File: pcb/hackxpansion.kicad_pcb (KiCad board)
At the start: 2 copper layers, 376 x 59.8 mm, 80 parts, among them CN1 533981471, CN2 533981471, CN3 533981471, CN4 533981471, IC1 ADS7128IRTET, J1 Conn_01x03_MountingPin, J2 USB_C_Receptacle_USB2.0_14P, Q1 BSS138, Q2 2N7002, SW1 SW_Push, SW2 SW_Push, SW3 SW_On_Off, U2 RP2354B, U5 SPX3819M5-L-3-3, U7 BQ24075RGT, Y1 ABM8-272-T3

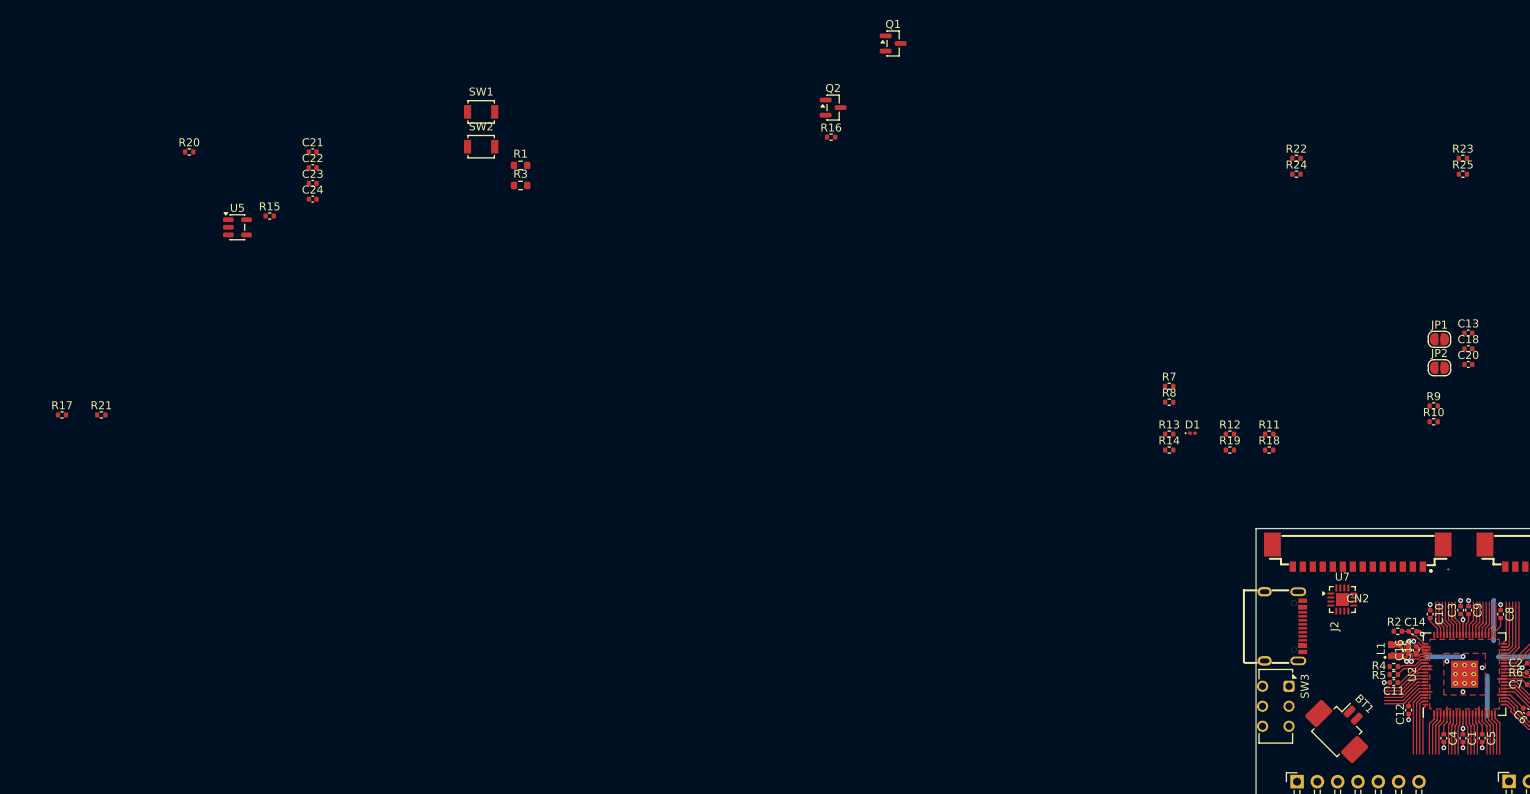
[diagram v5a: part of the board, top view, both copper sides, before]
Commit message: organized unlaid components
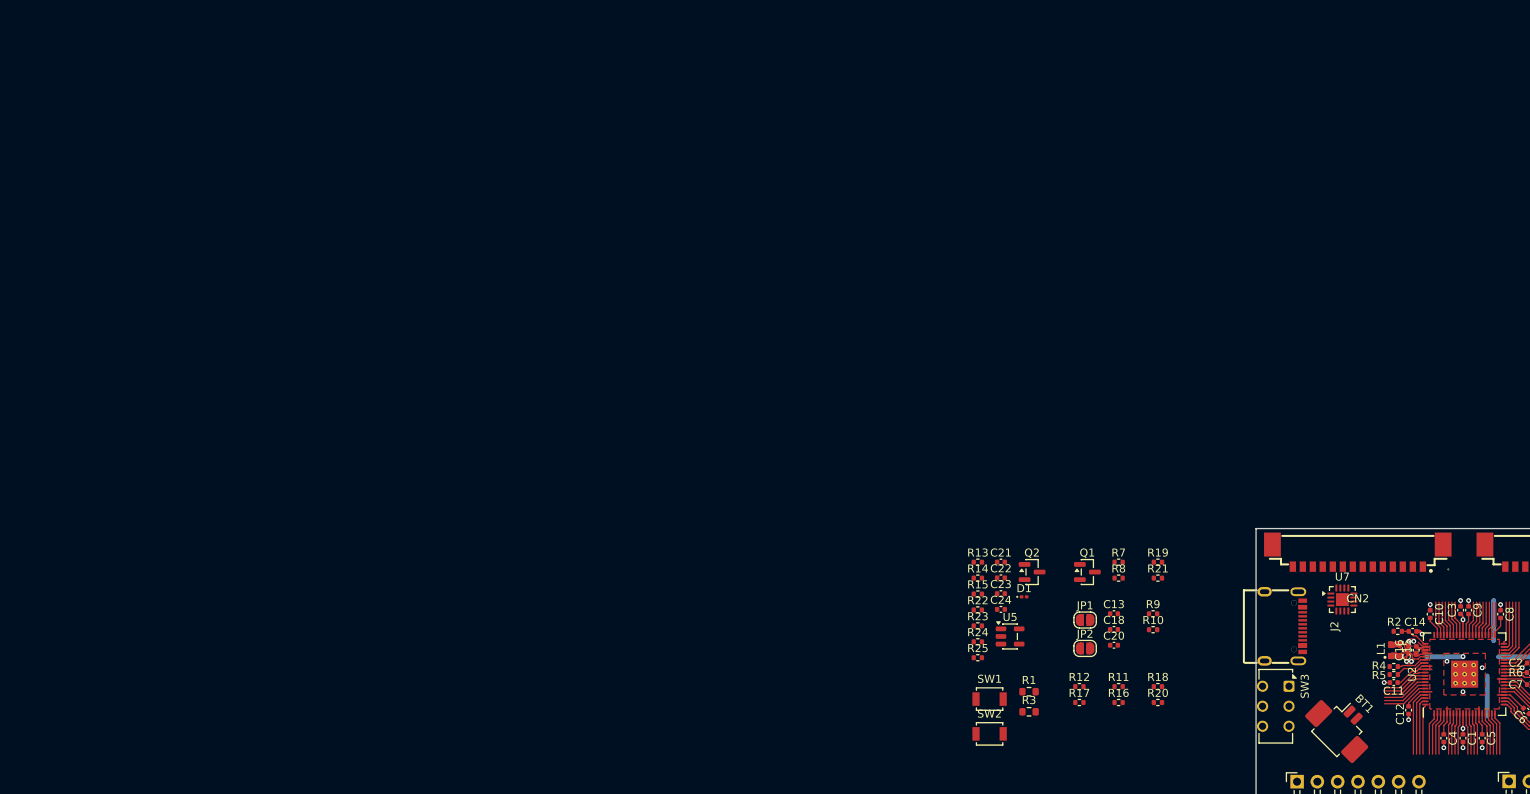
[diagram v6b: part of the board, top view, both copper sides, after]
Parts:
- moved R20 139.3 mm to (199.9, 108.1)
- moved R21 133.6 mm to (199.9, 92.6)
- moved R17 132.2 mm to (190.1, 108.1)
- moved U5 109.3 mm to (181.4, 99.8)
- moved R15 100.3 mm to (177.4, 94.5)
- moved C21 100.2 mm to (180.3, 90.6)
- moved C22 100.2 mm to (180.3, 92.5)
- moved C23 100.2 mm to (180.3, 94.5)
- moved C24 100.2 mm to (180.3, 96.5)
- moved SW1 97.1 mm to (178.8, 107.7)
- moved SW2 97.1 mm to (178.8, 112.0)
- moved R1 91.5 mm to (183.8, 106.8)
- moved R3 91.5 mm to (183.8, 109.3)
- moved R25 85.6 mm to (177.4, 102.5)
- moved R23 84.2 mm to (177.4, 98.5)
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
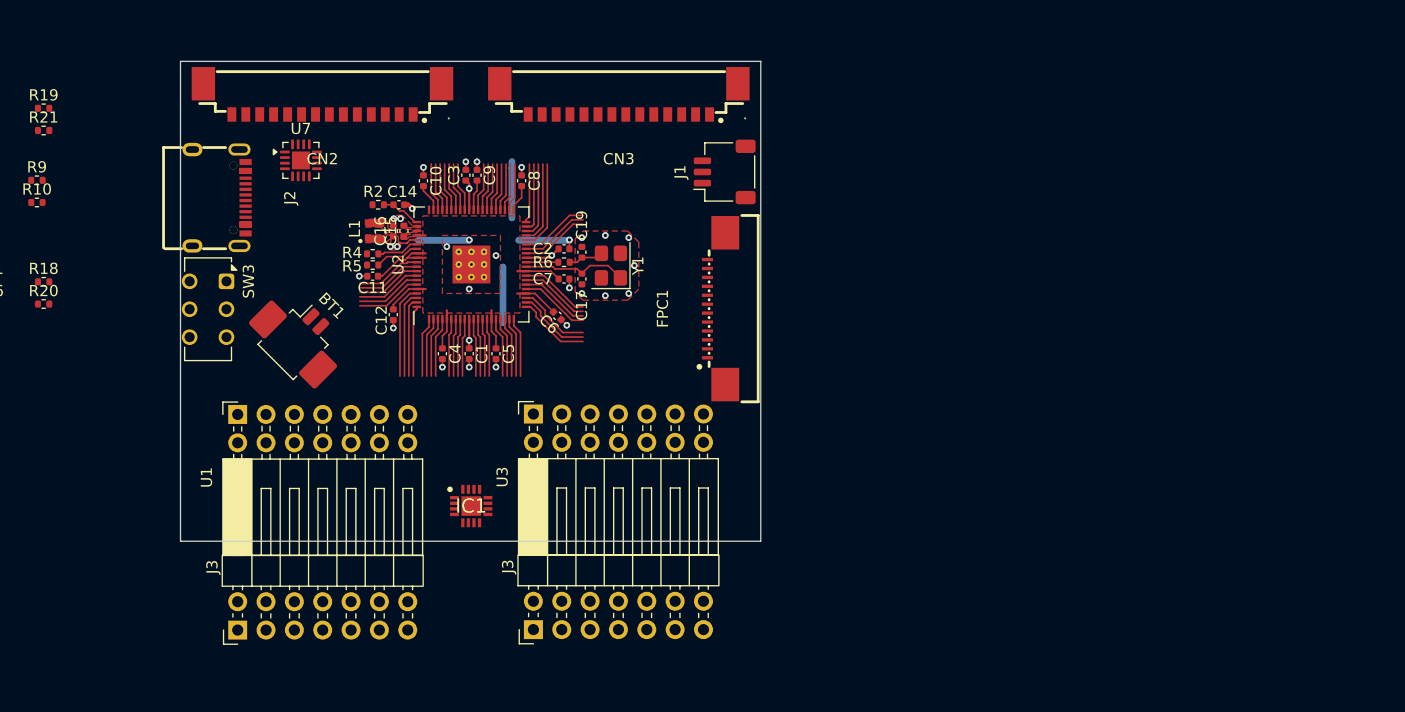
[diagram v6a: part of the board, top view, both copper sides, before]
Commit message: laid out edge components
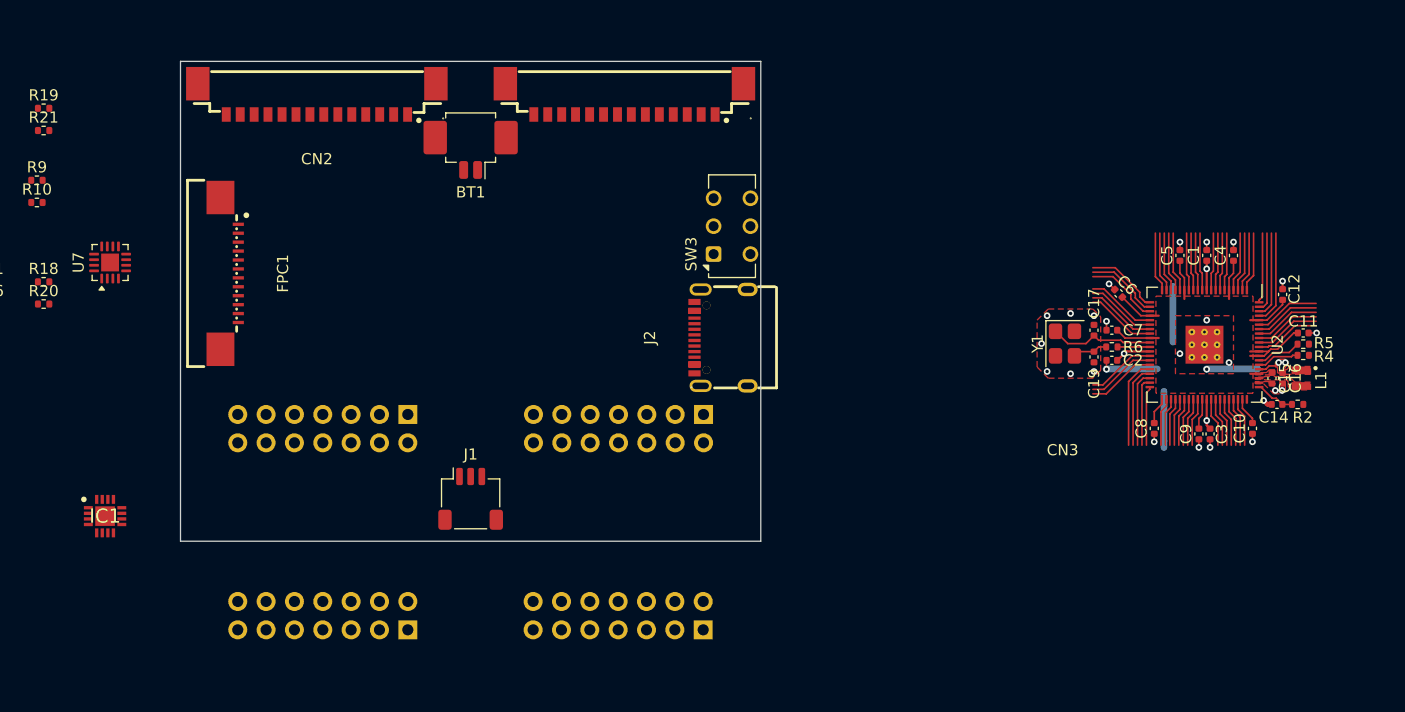
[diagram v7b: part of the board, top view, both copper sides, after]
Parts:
- J3 (x2), U1, U3: moved to B.Cu
- moved R2 84.3 mm to (312.3, 117.1), turned to 180 degrees
- moved L1 84.0 mm to (312.6, 114.8), turned to -90 degrees
- moved R4 83.9 mm to (312.8, 112.7), turned to 180 degrees
- moved R5 83.7 mm to (312.8, 111.7), turned to 180 degrees
- moved C11 83.5 mm to (312.8, 110.7), turned to 0 degrees
- moved C16 80.8 mm to (310.9, 114.8), turned to -90 degrees
- moved C14 80.7 mm to (310.4, 117.1), turned to 180 degrees
- moved C12 79.7 mm to (310.9, 107.2), turned to 90 degrees
- moved C15 78.9 mm to (310.0, 114.8), turned to -90 degrees
- moved C10 77.5 mm to (308.2, 119.3), turned to -90 degrees
- moved C4 71.4 mm to (306.5, 103.8), turned to 90 degrees
- moved C3 70.6 mm to (304.4, 119.7), turned to -90 degrees
- moved C9 68.7 mm to (303.4, 119.8), turned to -90 degrees
- moved C1 66.7 mm to (304.1, 103.8), turned to 90 degrees
- moved U2 66.1 mm to (303.9, 111.7), turned to -90 degrees
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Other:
- copper layers 2 -> 4

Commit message: did more layout, added 3d models
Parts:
- added JP3: SolderJumper_2_Open, Jumper:SolderJumper-2_P1.3mm_Open_RoundedPad1.0x1.5mm, F.Cu at (225.3, 114.1)
- D1: footprint LED_SMD:LED_0201_0603Metric -> LED_SMD:LED_0603_1608Metric
- R1, R3: footprint Resistor_SMD:R_0603_1608Metric -> Resistor_SMD:R_0402_1005Metric
- moved R25 84.6 mm to (261.7, 95.7), turned to 180 degrees
- moved R15 81.2 mm to (258.5, 98.1), turned to -90 degrees
- moved D1 80.3 mm to (263.4, 94.9), turned to 90 degrees
- moved R13 76.7 mm to (253.4, 100.5), turned to 180 degrees
- moved R14 76.3 mm to (253.4, 99.6)
- moved C24 75.8 mm to (256.0, 95.8), turned to 90 degrees
- moved SW1 74.7 mm to (250.7, 128.1)
- moved R1 74.5 mm to (255.1, 128.1)
- moved R23 73.3 mm to (250.5, 94.7)
- moved U5 72.2 mm to (253.5, 96.3)
- moved C23 70.5 mm to (250.7, 96.8), turned to 90 degrees
- moved C21 68.9 mm to (249.1, 93.7), turned to 180 degrees
- moved R22 67.9 mm to (245.2, 94.4), turned to 180 degrees
- moved R24 67.6 mm to (244.8, 95.4), turned to 180 degrees
- moved Q2 66.8 mm to (250.5, 99.4), turned to 180 degrees
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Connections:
- BT1 pad 1: /GND -> /MAIN_GND
- C1 pad 2: /GND -> /MAIN_GND
- C10 pad 2: /GND -> /MAIN_GND
- C11 pad 2: /GND -> /MAIN_GND
- C12 pad 2: /GND -> /MAIN_GND
- C13 pad 2: /GND -> /MAIN_GND
- C14 pad 2: /GND -> /MAIN_GND
- C15 pad 2: /GND -> /MAIN_GND
- C16 pad 2: /GND -> /MAIN_GND
- C17 pad 1: /GND -> /MAIN_GND
- C18 pad 2: /GND -> /MAIN_GND
- C19 pad 1: /GND -> /MAIN_GND
- C2 pad 2: /GND -> /MAIN_GND
- C20 pad 2: /GND -> /MAIN_GND
- C21 pad 1: /Main Board/Power/GND -> /MAIN_GND
- C22 pad 1: /Main Board/Power/GND -> /MAIN_GND
- C23 pad 1: /Main Board/Power/GND -> /MAIN_GND
- C24 pad 1: /Main Board/Power/GND -> /MAIN_GND
- C3 pad 2: /GND -> /MAIN_GND
- C4 pad 2: /GND -> /MAIN_GND
- C5 pad 2: /GND -> /MAIN_GND
- C6 pad 2: /GND -> /MAIN_GND
- C7 pad 2: /GND -> /MAIN_GND
- C8 pad 2: /GND -> /MAIN_GND
- C9 pad 2: /GND -> /MAIN_GND
- CN1 pad 14: /GND -> /DAUGHT_GND
- CN2 pad 14: /GND -> /MAIN_GND
- CN3 pad 14: /GND -> /MAIN_GND
- CN4 pad 14: /GND -> /DAUGHT_GND
- FPC1 pad 1: /GND -> /MAIN_GND
- FPC1 pad 12: /GND -> /MAIN_GND
- FPC1 pad 5: /GND -> /MAIN_GND
- FPC1 pad 6: /GND -> /MAIN_GND
- IC1 pad 17: /GND -> /MAIN_GND
- IC1 pad 9: /GND -> /MAIN_GND
- J1 pad 2: /GND -> /MAIN_GND
- J1 pad MP: /GND -> /MAIN_GND
- J2 pad A1: /GND -> /MAIN_GND
- J2 pad A12: /GND -> /MAIN_GND
- J2 pad B1: /GND -> /MAIN_GND
- J2 pad B12: /GND -> /MAIN_GND
- J2 pad SH: /GND -> /MAIN_GND
- JP1 pad 2: /GND -> /MAIN_GND
- Q1 pad 2: /GND -> /MAIN_GND
- Q2 pad 2: /Main Board/Power/GND -> /MAIN_GND
- R10 pad 2: /GND -> /MAIN_GND
- R11 pad 2: /GND -> /MAIN_GND
- R12 pad 2: /GND -> /MAIN_GND
- R14 pad 2: /Main Board/Power/GND -> /MAIN_GND
- R16 pad 2: /GND -> /MAIN_GND
- R17 pad 2: /GND -> /MAIN_GND
- R18 pad 2: /GND -> /DAUGHT_GND
- R19 pad 2: /GND -> /DAUGHT_GND
- R20 pad 2: /GND -> /DAUGHT_GND
- R21 pad 2: /GND -> /DAUGHT_GND
- R22 pad 2: /Main Board/Power/GND -> /MAIN_GND
- R23 pad 2: /Main Board/Power/GND -> /MAIN_GND
- R24 pad 2: /Main Board/Power/GND -> /MAIN_GND
- R8 pad 1: /Main Board/Display/BACKLIGHT -> Net-(JP3-A)
- R9 pad 2: /GND -> /MAIN_GND
- SW1 pad 1: /GND -> /MAIN_GND
- SW2 pad 1: /GND -> /MAIN_GND
- SW3 pad 1: /Main Board/Power/GND -> /MAIN_GND
- U1 pad 1: /GND -> /MAIN_GND
- U2 pad 62: /GND -> /MAIN_GND
- U2 pad 81: /GND -> /MAIN_GND
- U3 pad 1: /GND -> /MAIN_GND
- U4 pad 1: /GND -> /DAUGHT_GND
- U5 pad 2: /Main Board/Power/GND -> /MAIN_GND
- U6 pad 1: /GND -> /DAUGHT_GND
- U7 pad 17: /Main Board/Power/GND -> /MAIN_GND
- U7 pad 4: /Main Board/Power/GND -> /MAIN_GND
- U7 pad 5: /Main Board/Power/GND -> /MAIN_GND
- U7 pad 6: /Main Board/Power/VSW -> /Main Board/Power/REG-OUT
- U7 pad 8: /Main Board/Power/GND -> /MAIN_GND
- Y1 pad 2: /GND -> /MAIN_GND
- Y1 pad 4: /GND -> /MAIN_GND
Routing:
- net /MAIN_GND: track 0.00 -> 14.3 mm, vias 0 -> 22
- net /GND: track 14.3 -> 0.00 mm, vias 13 -> 0
- net /+3V3: track 34.3 -> 35.4 mm
- net (no net): vias 9 -> 0
- added copper zone on F.Cu, net /+3V3
- added copper zone on F.Cu, net /MAIN_GND
- removed copper zone on F.Cu, net Net-(U2-VREG_LX)
